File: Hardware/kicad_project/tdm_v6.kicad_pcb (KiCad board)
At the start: 4 copper layers, 65 x 100 mm, 139 parts, among them J1 line_in, J2 headphone_out, J3 battery, J4 DebugHeader, Q1 DMG2305UX-13, SW1 spst_4_pin_internal, SW10 spst_4_pin_internal, SW11 spst_4_pin_internal, SW12 spst_4_pin_internal, SW13 spst_4_pin_internal, SW14 spst_4_pin_internal, SW15 spst_4_pin_internal, SW16 spst_4_pin_internal, SW17 spst_4_pin_internal, SW18 spst_4_pin_internal, SW19 spst_4_pin_internal, SW2 spst_4_pin_internal, SW20 spst_4_pin_internal, SW21 spst_4_pin_internal, SW22 spst_4_pin_internal, SW23 spst_4_pin_internal, SW24 spst_4_pin_internal, SW25 spst_4_pin_internal, SW26 spst_4_pin_internal, SW3 spst_4_pin_internal, SW4 spst_4_pin_internal, SW5 spst_4_pin_internal, SW6 spst_4_pin_internal, SW7 spst_4_pin_internal, SW8 spst_4_pin_internal, SW9 spst_4_pin_internal, U2 Pico, U3 TLV320AIC3204, U4 SPWmicrophone, U5 MCP73831T-2ATI_OT

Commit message: update project with corrected schematic / pcb
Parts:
- removed C2, C3, C4, C5: 1u, RandomJunk:C_0402_NoSilk
- removed D1, D2, D3, D4, D5: D, RandomJunk:D_SOD-323F_less_silk
- removed LS1: Speaker, RandomJunk:CMS-181325
- removed OL1: OLED, kbd:OLED_v2
- added C39: .47u, RandomJunk:C_0603_nosilk, F.Cu at (80.5, 40.8)
- added C40: .1uF, RandomJunk:C_0603_nosilk, F.Cu at (78.5, 44.2)
- added C41: 1u, RandomJunk:C_0402_NoSilk, F.Cu at (72.0, 51.4)
- added C42: 10u, RandomJunk:C_0402_NoSilk, F.Cu at (73.3, 44.1)
- added C43: 10u, RandomJunk:C_0402_NoSilk, F.Cu at (81.8, 47.1)
- added C44: .47u, RandomJunk:C_0603_nosilk, F.Cu at (73.5, 41.6)
- added C45: .47u, RandomJunk:C_0603_nosilk, F.Cu at (77.5, 54.0)
- added C46: 10u, RandomJunk:C_0402_NoSilk, F.Cu at (82.0, 50.5)
- added C47: .47u, RandomJunk:C_0603_nosilk, F.Cu at (85.2, 52.0)
- added C48: 47uf, Capacitors_SMD:C_1206, F.Cu at (83.3, 40.6)
- added C49: 47uf, Capacitors_SMD:C_1206, F.Cu at (90.2, 40.5)
- added C50: 10u, RandomJunk:C_0402_NoSilk, F.Cu at (40.5, 56.9)
- added C51: 1u, RandomJunk:C_0402_NoSilk, F.Cu at (47.8, 56.6)
- added C52: 1u, RandomJunk:C_0402_NoSilk, F.Cu at (38.8, 72.0)
- added C53: 1u, RandomJunk:C_0402_NoSilk, F.Cu at (38.8, 70.5)
- added C54: 1u, RandomJunk:C_0402_NoSilk, F.Cu at (43.2, 56.4)
- added C55: 10u, RandomJunk:C_0402_NoSilk, F.Cu at (52.8, 56.6)
- added C56: 10u, RandomJunk:C_0402_NoSilk, F.Cu at (49.0, 71.6)
- added C57: 10u, RandomJunk:C_0402_NoSilk, F.Cu at (48.6, 47.0)
- added C58: 10u, RandomJunk:C_0402_NoSilk, F.Cu at (40.2, 40.4)
- added D53: D_Schottky, Diodes_SMD:D_SMA, F.Cu at (56.5, 39.6)
- added D54: LED, LEDs:LED_0603, F.Cu at (57.8, 34.1)
- added J5: midi_in, RandomJunk:HRO-PJ-327C-A, B.Cu at (44.3, 40.6)
- added J6: midi_out, RandomJunk:HRO-PJ-327C-A, B.Cu at (54.3, 40.6)
- added J7: battery, Connectors_JST:JST_PH_B2B-PH-SM4-TB_02x2.00mm_Straight, B.Cu at (50.8, 52.1)
- added LCD1: 128x32OLED, RandomJunk:oled_ssd1306_14pin_91, F.Cu at (43.3, 62.1)
- added R10: 220, RandomJunk:R_0402_NoSilk, F.Cu at (40.7, 44.5)
- added R11: 1k, RandomJunk:R_0402_NoSilk, F.Cu at (44.5, 56.5)
- added R12: 220, RandomJunk:R_0402_NoSilk, F.Cu at (50.2, 37.6)
- added R13: 220, RandomJunk:R_0402_NoSilk, F.Cu at (56.0, 42.0)
- added R14: 10k, RandomJunk:R_0402_NoSilk, F.Cu at (50.3, 56.6)
- added R15: 330k, RandomJunk:R_0402_NoSilk, F.Cu at (48.5, 70.1)
- added R16: 4.7k, RandomJunk:R_0402_NoSilk, F.Cu at (52.4, 42.9)
- added R17: 1k, RandomJunk:R_0402_NoSilk, F.Cu at (55.8, 33.1)
- added R18: 100k, RandomJunk:R_0402_NoSilk, F.Cu at (52.4, 44.0)
- added R19: 5.1k, RandomJunk:R_0402_NoSilk, F.Cu at (66.8, 42.1)
- added R20: 5.1k, RandomJunk:R_0402_NoSilk, F.Cu at (63.3, 42.1)
- added R7: 1k, RandomJunk:R_0402_NoSilk, F.Cu at (67.5, 48.4)
- added R8: 1k, RandomJunk:R_0402_NoSilk, F.Cu at (59.8, 42.5)
- added R9: 4.7k, RandomJunk:R_0402_NoSilk, F.Cu at (79.5, 53.8)
- added SW27: spst_4_pin_internal, RandomJunk:ts1102_smallerpads_buttonhole, B.Cu at (60.8, 67.6)
- added U1: W25Q32JVSS, Housings_SOIC:SOIJ-8_5.3x5.3mm_Pitch1.27mm, F.Cu at (49.7, 50.5)
- added U6: MCP73831T-2ATI_OT, TO_SOT_Packages_SMD:SOT-23-5, F.Cu at (51.1, 40.4)
- added U7: AMS1117-3.3, TO_SOT_Packages_SMD:SOT-223, F.Cu at (44.4, 37.1)
- added Y1: Crystal_GND24, Crystals:Crystal_SMD_3225-4pin_3.2x2.5mm, F.Cu at (70.5, 48.5)
- C1: footprint RandomJunk:C_0402_NoSilk -> Capacitors_SMD:C_0402_NoSilk
- C26, C30, C31, C34: value 10u -> 100n; footprint RandomJunk:C_0603_nosilk -> RandomJunk:C_0402_NoSilk
- C27, C32: value .47u -> 100n; footprint RandomJunk:C_0603_nosilk -> RandomJunk:C_0402_NoSilk
- C28: value .1uF -> 100n; footprint RandomJunk:C_0603_nosilk -> RandomJunk:C_0402_NoSilk
- C29: value 1.0u -> 100n; footprint RandomJunk:C_0603_nosilk -> RandomJunk:C_0402_NoSilk
- C33: value .47u -> 1u; footprint RandomJunk:C_0603_nosilk -> RandomJunk:C_0402_NoSilk
- C35: value .47u -> 30p; footprint RandomJunk:C_0603_nosilk -> RandomJunk:C_0402_NoSilk
- C36: value 47uf -> 10u; footprint Capacitors_SMD:C_1206 -> RandomJunk:C_0402_NoSilk
- C37: value 47uf -> 30p; footprint Capacitors_SMD:C_1206 -> RandomJunk:C_0402_NoSilk
- C38: footprint RandomJunk:C_0603_nosilk -> RandomJunk:C_0402_NoSilk
- D10, D11, D12, D13, D14, D15, D16, D17, D18, D19, D20, D21, D22, D23, D24, D25, D6, D7, D8, D9: value D -> WS2812B; footprint RandomJunk:D_SOD-323F_less_silk -> RandomJunk:ws2812b-2020-lightpipe
- D26, D27, D28, D29, D30, D31, D32, D33, D34, D35, D36, D37, D38, D39, D40, D41, D42, D43, D44, D45, D46, D47, D48, D49, D50: value WS2812B -> D; footprint RandomJunk:ws2812b-2020-lightpipe -> RandomJunk:D_SOD-323F_less_silk
- D51: value D_Schottky -> LED; footprint Diodes_SMD:D_SMA -> LEDs:LED_0603
- D52: value LED -> D; footprint LEDs:LED_0603 -> RandomJunk:D_SOD-323F_less_silk
- J1: value line_in -> picoprobe_debug; footprint RandomJunk:HRO-PJ-327C-A -> RandomJunk:pico debug header; moved to B.Cu
- J2: value headphone_out -> USB_C_Receptacle_USB2.0; footprint RandomJunk:HRO-PJ-327C-A -> RandomJunk:USB-C_SMD-TYPE-C-31-M-12
- J3: value battery -> line_in; footprint Connectors_JST:JST_PH_B2B-PH-SM4-TB_02x2.00mm_Straight -> RandomJunk:HRO-PJ-327C-A
- J4: value DebugHeader -> headphone_out; footprint Connector_PinSocket_2.54mm:PinSocket_1x04_P2.54mm_Vertical -> RandomJunk:HRO-PJ-327C-A
- R1, R2: value 4.7k -> 27.4; footprint Resistors_SMD:R_0603 -> RandomJunk:R_0402_NoSilk
- R3: value 4.7k -> DNF; footprint Resistors_SMD:R_0603 -> RandomJunk:R_0402_NoSilk
- R4: footprint Resistors_SMD:R_0603 -> RandomJunk:R_0402_NoSilk
- R5: value 1k -> 4.7k; footprint Resistors_SMD:R_0603 -> RandomJunk:R_0402_NoSilk
- R6: value 100k -> 1k; footprint Resistors_SMD:R_0603 -> RandomJunk:R_0402_NoSilk
- RV1, RV2: footprint RandomJunk:rk10j -> Potentiometers:Potentiometer_Alps_RK09K_Horizontal; moved to F.Cu
- SW26: moved to B.Cu
- U2: value Pico -> RP2040; footprint RandomJunk:RPi_Pico_SMD_only -> MCU_RaspberryPi_and_Boards:RP2040-QFN-56; moved to F.Cu
- U4: value SPWmicrophone -> AP3722AT_mic; footprint RandomJunk:SPW2430HR5H-B -> RandomJunk:AP3722AT-SMD-mic
- U5: value MCP73831T-2ATI_OT -> 6N137; footprint TO_SOT_Packages_SMD:SOT-23-5 -> Housings_SOIC:SO-8_5.3x6.2mm_Pitch1.27mm
- moved J1 93.6 mm to (65.8, 130.0), turned to 0 degrees
- moved H1 92.4 mm to (37.3, 128.1)
- moved H3 92.4 mm to (94.3, 128.1)
- moved H2 91.7 mm to (37.3, 35.6)
- moved H4 91.7 mm to (94.3, 35.6)
- moved U4 48.2 mm to (88.7, 50.6), turned to 90 degrees
- moved U5 48.0 mm to (39.2, 51.3), turned to 270 degrees
- moved J4 43.6 mm to (86.8, 40.6)
- moved RV1 39.1 mm to (73.8, 56.1)
- moved D51 38.1 mm to (61.3, 42.6), turned to 270 degrees
- moved Q1 36.8 mm to (49.2, 44.4), turned to 270 degrees
- moved SW26 32.0 mm to (60.8, 60.6), turned to 180 degrees
- moved R6 31.9 mm to (55.8, 54.7), turned to 270 degrees
- moved R4 29.5 mm to (60.3, 55.6), turned to 90 degrees
- moved U3 29.3 mm to (76.8, 49.1), turned to 0 degrees
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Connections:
- C1 pad 1: +3V3 -> Net-(C1-Pad1)
- C26 pad 1: GND -> +3V3
- C26 pad 2: Net-(C26-Pad2) -> GND
- C27 pad 1: Net-(C27-Pad1) -> +3V3
- C27 pad 2: Net-(C27-Pad2) -> GND
- C31 pad 1: Net-(C31-Pad1) -> +3V3
- C32 pad 1: Net-(C32-Pad1) -> +3V3
- C32 pad 2: Net-(C32-Pad2) -> GND
- C33 pad 1: Net-(C33-Pad1) -> +3V3
- C33 pad 2: Net-(C33-Pad2) -> GND
- C34 pad 1: GND -> +3V3
- C34 pad 2: Net-(C34-Pad2) -> GND
- C35 pad 1: Net-(C35-Pad1) -> /XIN
- C35 pad 2: Net-(C35-Pad2) -> GND
- C36 pad 1: Net-(C36-Pad1) -> VBUS
- C36 pad 2: Net-(C36-Pad2) -> GND
- C37 pad 2: Net-(C37-Pad2) -> GND
- C38 pad 1: +BATT -> GND
- C38 pad 2: GND -> Net-(C38-Pad2)
- D10 pad 1: key_row2 -> Net-(D10-Pad1)
- D10 pad 2: Net-(D10-Pad2) -> GND
- D11 pad 1: key_row3 -> Net-(D11-Pad1)
- D11 pad 2: Net-(D11-Pad2) -> GND
- D12 pad 1: key_row3 -> Net-(D12-Pad1)
- D12 pad 2: Net-(D12-Pad2) -> GND
- D13 pad 1: key_row3 -> Net-(D13-Pad1)
- D13 pad 2: Net-(D13-Pad2) -> GND
- D14 pad 1: key_row3 -> Net-(D14-Pad1)
- D14 pad 2: Net-(D14-Pad2) -> GND
- D15 pad 1: key_row3 -> Net-(D15-Pad1)
- D15 pad 2: Net-(D15-Pad2) -> GND
- D16 pad 1: key_row4 -> Net-(D16-Pad1)
- D16 pad 2: Net-(D16-Pad2) -> GND
- D17 pad 1: key_row4 -> Net-(D17-Pad1)
- D17 pad 2: Net-(D17-Pad2) -> GND
- D18 pad 1: key_row4 -> Net-(D18-Pad1)
- D18 pad 2: Net-(D18-Pad2) -> GND
- D19 pad 1: key_row4 -> Net-(D19-Pad1)
- D19 pad 2: Net-(D19-Pad2) -> GND
- D20 pad 1: key_row4 -> Net-(D20-Pad1)
- D20 pad 2: Net-(D20-Pad2) -> GND
- D21 pad 1: key_row5 -> Net-(D21-Pad1)
- D21 pad 2: Net-(D21-Pad2) -> GND
- D22 pad 1: key_row5 -> Net-(D22-Pad1)
- D22 pad 2: Net-(D22-Pad2) -> GND
- D23 pad 1: key_row5 -> Net-(D23-Pad1)
- D23 pad 2: Net-(D23-Pad2) -> GND
- D24 pad 1: key_row5 -> Net-(D24-Pad1)
- D24 pad 2: Net-(D24-Pad2) -> GND
- D25 pad 1: key_row5 -> Net-(D25-Pad1)
- D25 pad 2: Net-(D25-Pad2) -> GND
- D26 pad 1: Net-(D26-Pad1) -> key_row1
- D26 pad 2: GND -> Net-(D26-Pad2)
- D27 pad 1: Net-(D27-Pad1) -> key_row1
- D27 pad 2: GND -> Net-(D27-Pad2)
- D28 pad 1: Net-(D28-Pad1) -> key_row1
- D28 pad 2: GND -> Net-(D28-Pad2)
- D29 pad 1: Net-(D29-Pad1) -> key_row1
- D29 pad 2: GND -> Net-(D29-Pad2)
- D30 pad 1: Net-(D30-Pad1) -> key_row1
- D30 pad 2: GND -> Net-(D30-Pad2)
- D31 pad 1: Net-(D31-Pad1) -> key_row2
- D31 pad 2: GND -> Net-(D31-Pad2)
- D32 pad 1: Net-(D32-Pad1) -> key_row2
- D32 pad 2: GND -> Net-(D32-Pad2)
- D33 pad 1: Net-(D33-Pad1) -> key_row2
- D33 pad 2: GND -> Net-(D33-Pad2)
- D34 pad 1: Net-(D34-Pad1) -> key_row2
- D34 pad 2: GND -> Net-(D34-Pad2)
- D35 pad 1: Net-(D35-Pad1) -> key_row2
- D35 pad 2: GND -> Net-(D35-Pad2)
- D36 pad 1: Net-(D36-Pad1) -> key_row3
- D36 pad 2: GND -> Net-(D36-Pad2)
- D37 pad 1: Net-(D37-Pad1) -> key_row3
- D37 pad 2: GND -> Net-(D37-Pad2)
- D38 pad 1: Net-(D38-Pad1) -> key_row3
- D38 pad 2: GND -> Net-(D38-Pad2)
- D39 pad 1: Net-(D39-Pad1) -> key_row3
- D39 pad 2: GND -> Net-(D39-Pad2)
- D40 pad 1: Net-(D40-Pad1) -> key_row3
- D40 pad 2: GND -> Net-(D40-Pad2)
- D41 pad 1: Net-(D41-Pad1) -> key_row4
- D41 pad 2: GND -> Net-(D41-Pad2)
- D42 pad 1: Net-(D42-Pad1) -> key_row4
- D42 pad 2: GND -> Net-(D42-Pad2)
- D43 pad 1: Net-(D43-Pad1) -> key_row4
- D43 pad 2: GND -> Net-(D43-Pad2)
- D44 pad 1: Net-(D44-Pad1) -> key_row4
- D44 pad 2: GND -> Net-(D44-Pad2)
- D45 pad 1: Net-(D45-Pad1) -> key_row4
- D45 pad 2: GND -> Net-(D45-Pad2)
- D46 pad 1: Net-(D46-Pad1) -> key_row5
- D46 pad 2: GND -> Net-(D46-Pad2)
- D47 pad 1: Net-(D47-Pad1) -> key_row5
- D47 pad 2: GND -> Net-(D47-Pad2)
- D48 pad 1: Net-(D48-Pad1) -> key_row5
- D48 pad 2: GND -> Net-(D48-Pad2)
- D49 pad 1: Net-(D49-Pad1) -> key_row5
- D49 pad 2: GND -> Net-(D49-Pad2)
- D50 pad 1: (no net) -> key_row5
- D50 pad 2: GND -> Net-(D50-Pad2)
- D51 pad 1: vsys -> Net-(D51-Pad1)
- D51 pad 2: VBUS -> Net-(D51-Pad2)
- D52 pad 2: VBUS -> Net-(D52-Pad2)
- D6 pad 1: key_row2 -> Net-(D6-Pad1)
- D6 pad 2: Net-(D6-Pad2) -> GND
- D7 pad 1: key_row2 -> Net-(D7-Pad1)
- D7 pad 2: Net-(D7-Pad2) -> GND
- D8 pad 1: key_row2 -> Net-(D8-Pad1)
- D8 pad 2: Net-(D8-Pad2) -> GND
- D9 pad 1: key_row2 -> Net-(D10-Pad3)
- D9 pad 2: Net-(D9-Pad2) -> GND
- J1 pad 2: Net-(C27-Pad2) -> swclk
- J1 pad 3: Net-(C32-Pad2) -> swdio
- J1 pad 4: (no net) -> rx
- J3 pad 1: +BATT -> GND
- J3 pad 2: GND -> Net-(C39-Pad2)
- J4 pad 1: Net-(J4-Pad1) -> GND
- J4 pad 2: Net-(J4-Pad2) -> Net-(C49-Pad1)
- J4 pad 3: Net-(J4-Pad3) -> Net-(C48-Pad1)
- Q1 pad 2: vsys -> Net-(D53-Pad1)
- R1 pad 1: +3V3 -> Net-(R1-Pad1)
- R1 pad 2: sda -> /USB_D+
- R2 pad 1: +3V3 -> Net-(R2-Pad1)
- R2 pad 2: scl -> /USB_D-
- R3 pad 1: Net-(C33-Pad2) -> +3V3
- R3 pad 2: Net-(R3-Pad2) -> /QSPI_SS
- R4 pad 1: Net-(R4-Pad1) -> +3V3
- R4 pad 2: GND -> sda
- R5 pad 1: Net-(D52-Pad1) -> +3V3
- R5 pad 2: Net-(R5-Pad2) -> scl
- R6 pad 1: GND -> /QSPI_SS
- R6 pad 2: VBUS -> Net-(R6-Pad2)
- SW1 pad 1: Net-(D1-Pad2) -> Net-(D26-Pad2)
- SW1 pad 2: (no net) -> Net-(SW1-Pad2)
- SW10 pad 1: Net-(D10-Pad2) -> Net-(D35-Pad2)
- SW10 pad 2: (no net) -> Net-(SW10-Pad2)
- SW11 pad 1: Net-(D11-Pad2) -> Net-(D36-Pad2)
- SW11 pad 2: (no net) -> Net-(SW11-Pad2)
- SW12 pad 1: Net-(D12-Pad2) -> Net-(D37-Pad2)
- SW12 pad 2: (no net) -> Net-(SW12-Pad2)
- SW13 pad 1: Net-(D13-Pad2) -> Net-(D38-Pad2)
- SW13 pad 2: (no net) -> Net-(SW13-Pad2)
- SW14 pad 1: Net-(D14-Pad2) -> Net-(D39-Pad2)
- SW14 pad 2: (no net) -> Net-(SW14-Pad2)
- SW15 pad 1: Net-(D15-Pad2) -> Net-(D40-Pad2)
- SW15 pad 2: (no net) -> Net-(SW15-Pad2)
- SW16 pad 1: Net-(D16-Pad2) -> Net-(D41-Pad2)
- SW16 pad 2: (no net) -> Net-(SW16-Pad2)
- SW17 pad 1: Net-(D17-Pad2) -> Net-(D42-Pad2)
- SW17 pad 2: (no net) -> Net-(SW17-Pad2)
- SW18 pad 1: Net-(D18-Pad2) -> Net-(D43-Pad2)
- SW18 pad 2: (no net) -> Net-(SW18-Pad2)
- SW19 pad 1: Net-(D19-Pad2) -> Net-(D44-Pad2)
- SW19 pad 2: (no net) -> Net-(SW19-Pad2)
- SW2 pad 1: Net-(D2-Pad2) -> Net-(D27-Pad2)
- SW2 pad 2: (no net) -> Net-(SW2-Pad2)
- SW20 pad 1: Net-(D20-Pad2) -> Net-(D45-Pad2)
- SW20 pad 2: (no net) -> Net-(SW20-Pad2)
- SW21 pad 1: Net-(D21-Pad2) -> Net-(D46-Pad2)
- SW21 pad 2: (no net) -> Net-(SW21-Pad2)
- SW21 pad 3: (no net) -> Net-(SW21-Pad3)
- SW22 pad 1: Net-(D22-Pad2) -> Net-(D47-Pad2)
- SW22 pad 2: (no net) -> Net-(SW22-Pad2)
- SW22 pad 3: (no net) -> Net-(SW22-Pad3)
- SW23 pad 1: Net-(D23-Pad2) -> Net-(D48-Pad2)
- SW23 pad 2: (no net) -> Net-(SW23-Pad2)
- SW23 pad 3: (no net) -> Net-(SW23-Pad3)
- SW24 pad 1: Net-(D24-Pad2) -> Net-(D49-Pad2)
- SW24 pad 2: (no net) -> Net-(SW24-Pad2)
- SW24 pad 3: (no net) -> Net-(SW24-Pad3)
- SW25 pad 1: Net-(D25-Pad2) -> Net-(D50-Pad2)
- SW25 pad 2: (no net) -> Net-(SW25-Pad2)
- SW25 pad 3: (no net) -> Net-(SW25-Pad3)
- SW26 pad 2: (no net) -> Net-(R6-Pad2)
- SW26 pad 4: (no net) -> Net-(SW26-Pad4)
- SW3 pad 1: Net-(D3-Pad2) -> Net-(D28-Pad2)
- SW3 pad 2: (no net) -> Net-(SW3-Pad2)
- SW4 pad 1: Net-(D4-Pad2) -> Net-(D29-Pad2)
- SW4 pad 2: (no net) -> Net-(SW4-Pad2)
- SW5 pad 1: Net-(D5-Pad2) -> Net-(D30-Pad2)
- SW5 pad 2: (no net) -> Net-(SW5-Pad2)
- SW6 pad 1: Net-(D6-Pad2) -> Net-(D31-Pad2)
- SW6 pad 2: (no net) -> Net-(SW6-Pad2)
- SW7 pad 1: Net-(D7-Pad2) -> Net-(D32-Pad2)
- SW7 pad 2: (no net) -> Net-(SW7-Pad2)
- SW8 pad 1: Net-(D8-Pad2) -> Net-(D33-Pad2)
- SW8 pad 2: (no net) -> Net-(SW8-Pad2)
- SW9 pad 1: Net-(D9-Pad2) -> Net-(D34-Pad2)
- SW9 pad 2: (no net) -> Net-(SW9-Pad2)
- U2 pad 1: Net-(J4-Pad4) -> +3V3
- U2 pad 10: key_col2 -> +3V3
- U2 pad 13: (no net) -> key_col5
- U2 pad 14: key_col5 -> key_row1
- U2 pad 15: key_row1 -> key_row2
- U2 pad 16: key_row2 -> key_row3
- U2 pad 17: key_row3 -> key_row4
- U2 pad 18: (no net) -> key_row5
- U2 pad 19: key_row4 -> GND
- U2 pad 2: Net-(J4-Pad3) -> tx
- U2 pad 20: key_row5 -> /XIN
- U2 pad 21: mclk -> /XOUT
- U2 pad 22: bck -> +3V3
- U2 pad 23: GND -> Net-(C1-Pad1)
- U2 pad 24: lrclk -> swclk
- U2 pad 25: din -> swdio
- U2 pad 26: dout -> Net-(SW27-Pad1)
- U2 pad 27: codec_reset -> mclk
- U2 pad 28: GND -> bck
- U2 pad 29: (no net) -> lrclk
- U2 pad 3: (no net) -> rx
- U2 pad 30: Net-(SW26-Pad1) -> din
- U2 pad 31: pot1 -> dout
- U2 pad 32: pot2 -> codec_reset
- U2 pad 33: (no net) -> +3V3
- U2 pad 34: (no net) -> led_din
- U2 pad 35: (no net) -> Net-(U2-Pad35)
- U2 pad 36: +3V3 -> Net-(U2-Pad36)
- U2 pad 37: (no net) -> Net-(D51-Pad2)
- U2 pad 38: GND -> pot1
- U2 pad 39: vsys -> pot2
- U2 pad 40: VBUS -> Net-(U2-Pad40)
- U2 pad 41: Net-(J4-Pad2) -> Net-(U2-Pad41)
- U2 pad 42: (no net) -> +3V3
- U2 pad 43: Net-(J4-Pad1) -> +3V3
- U2 pad 6: led_din -> /MIDI_TX
- U2 pad 7: (no net) -> /MIDI_RX
- U2 pad 8: (no net) -> key_col1
- U2 pad 9: key_col1 -> key_col2
- U3 pad 11: (no net) -> Net-(U3-Pad11)
- U3 pad 13: Net-(C27-Pad1) -> Net-(C39-Pad1)
- U3 pad 14: Net-(C32-Pad1) -> Net-(C44-Pad1)
- U3 pad 15: Net-(C33-Pad1) -> Net-(C45-Pad1)
- U3 pad 16: Net-(C35-Pad1) -> Net-(C47-Pad1)
- U3 pad 18: Net-(C34-Pad2) -> Net-(C46-Pad2)
- U3 pad 19: Net-(R3-Pad2) -> Net-(R9-Pad2)
- U3 pad 20: (no net) -> Net-(U3-Pad20)
- U3 pad 21: (no net) -> Net-(U3-Pad21)
- U3 pad 22: (no net) -> Net-(U3-Pad22)
- U3 pad 23: (no net) -> Net-(U3-Pad23)
- U3 pad 24: Net-(C31-Pad1) -> Net-(C43-Pad1)
- U3 pad 25: Net-(C37-Pad2) -> Net-(C49-Pad2)
- U3 pad 27: Net-(C36-Pad2) -> Net-(C48-Pad2)
- U3 pad 29: Net-(C26-Pad2) -> Net-(C38-Pad2)
- U3 pad 32: (no net) -> Net-(U3-Pad32)
- U3 pad 8: (no net) -> Net-(U3-Pad8)
- U4 pad 1: GND -> Net-(C45-Pad2)
- U4 pad 2: Net-(C33-Pad2) -> GND
- U4 pad 3: Net-(C35-Pad2) -> GND
- U4 pad 4: (no net) -> Net-(C47-Pad2)
- U5 pad 1: Net-(R5-Pad2) -> Net-(U5-Pad1)
- U5 pad 2: GND -> Net-(D52-Pad1)
- U5 pad 3: +BATT -> Net-(D52-Pad2)
- U5 pad 4: VBUS -> Net-(U5-Pad4)
- U5 pad 5: Net-(R4-Pad1) -> GND
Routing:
- net +3V3: track 140.2 -> 354.0 mm, vias 53 -> 46
- net swdio: track 0.00 -> 94.1 mm, vias 0 -> 2
- net tx: track 0.00 -> 90.6 mm, vias 0 -> 1
- net rx: track 0.00 -> 89.7 mm, vias 0 -> 1
- net swclk: track 0.00 -> 89.1 mm, vias 0 -> 2
- net scl: track 127.5 -> 45.2 mm
- net Net-(D30-Pad1): track 70.9 -> 0.00 mm
- net GND: track 167.6 -> 238.4 mm, vias 34 -> 22
- net Net-(D35-Pad1): track 60.6 -> 0.00 mm, vias 2 -> 0
- net Net-(D45-Pad1): track 60.1 -> 0.00 mm, vias 2 -> 0
- net vsys: track 56.5 -> 0.00 mm, vias 3 -> 0
- net Net-(J4-Pad2): track 55.8 -> 0.00 mm, vias 4 -> 0
- net Net-(D40-Pad1): track 54.3 -> 0.00 mm, vias 2 -> 0
- net Net-(D20-Pad1): track 0.00 -> 53.3 mm
- net Net-(D15-Pad1): track 0.00 -> 53.3 mm
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- added copper zone on B.Cu, net +3V3
- added copper zone on B.Cu, net GND
- added copper zone on F.Cu, net GND
- added copper zone on In2.Cu, net GND
- removed copper zone on In2.Cu, net +3V3
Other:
- outline, holes or cut-outs redrawn
- rule trace_min: 0.2 -> 0.09
- rule via_min_drill: 0.3 -> 0.2
- board text added: "+"
- board text added: "Audio In"
- board text added: "Audio Out"
- board text added: "RUN"
- board text added: "SAFEBOOT"
- board text added: "audio codec"
- board text added: "battery"
- board text added: "charge indicator"
- board text added: "crystal"
- board text added: "mcu"
- board text added: "memory"
- board text added: "mic ro phone"
- board text added: "midi optoiso"
- board text added: "power"

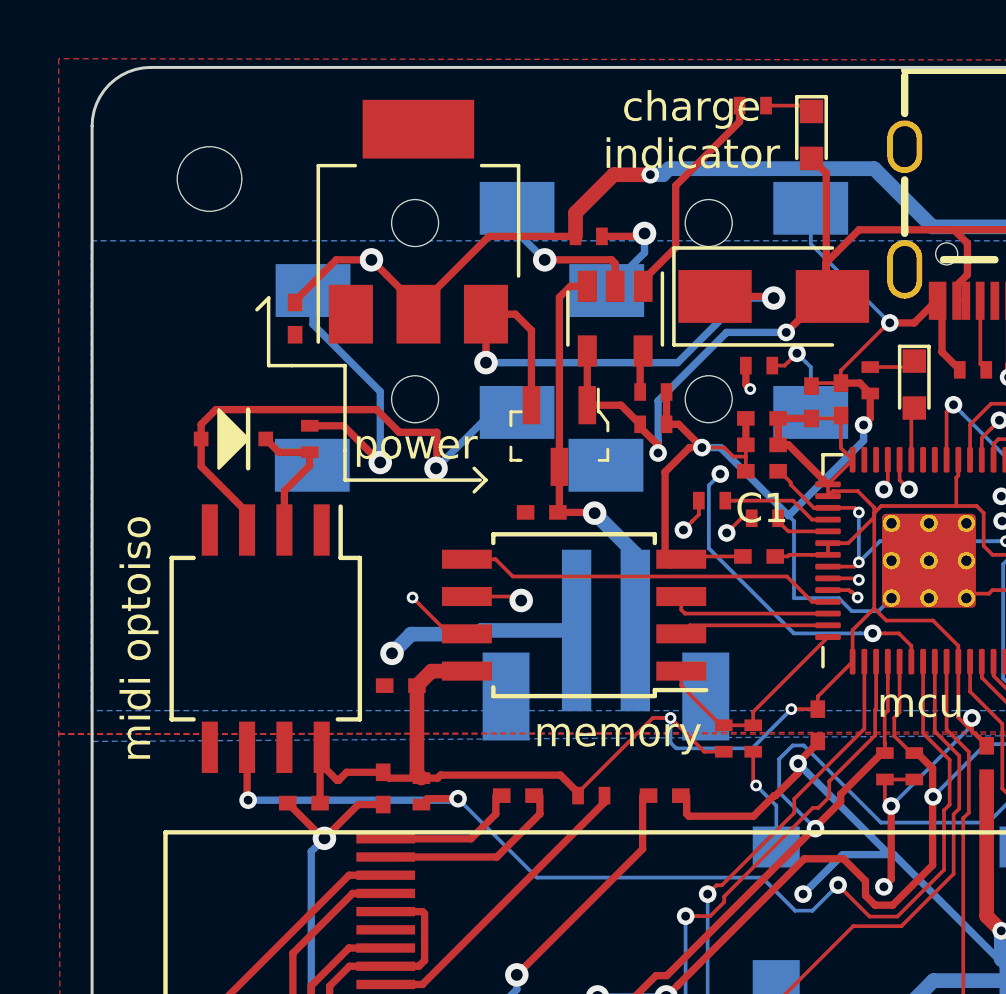
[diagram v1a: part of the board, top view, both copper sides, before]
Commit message: initial firmware commit, update hardware
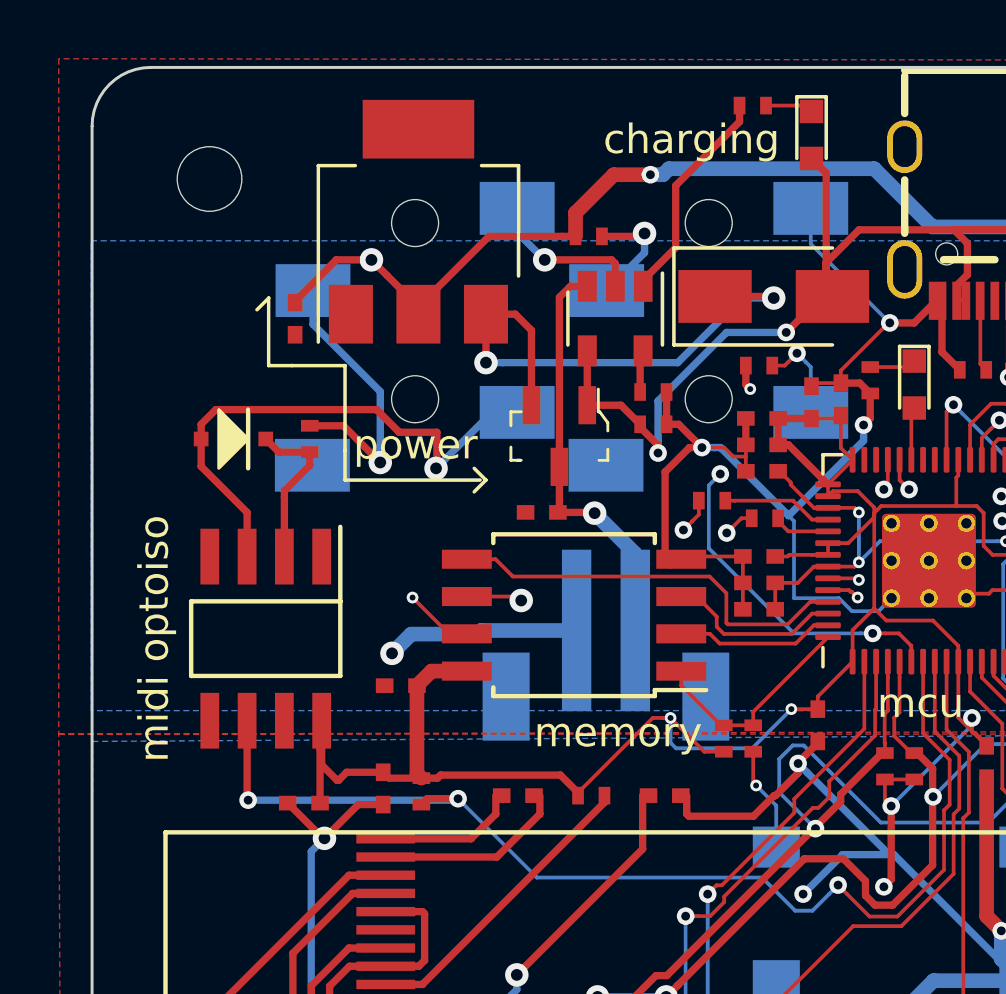
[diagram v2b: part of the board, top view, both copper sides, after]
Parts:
- added C2: 100n, Capacitors_SMD:C_0402_NoSilk, F.Cu at (56.0, 50.3)
- added C3: 100n, Capacitors_SMD:C_0402_NoSilk, F.Cu at (56.0, 49.4)
- U5: footprint Housings_SOIC:SO-8_5.3x6.2mm_Pitch1.27mm -> RandomJunk:SOP-8_3.9x5.1x1.27P
- turned U5 to 180 degrees
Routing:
- net Net-(C1-Pad1): track 12.3 -> 15.3 mm
- net GND: track 238.4 -> 240.2 mm
- net /QSPI_SD0: track 12.9 -> 14.1 mm
- net /QSPI_SD2: track 5.50 -> 6.02 mm
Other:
- board text added: "charging"
- board text removed: "charge indicator"

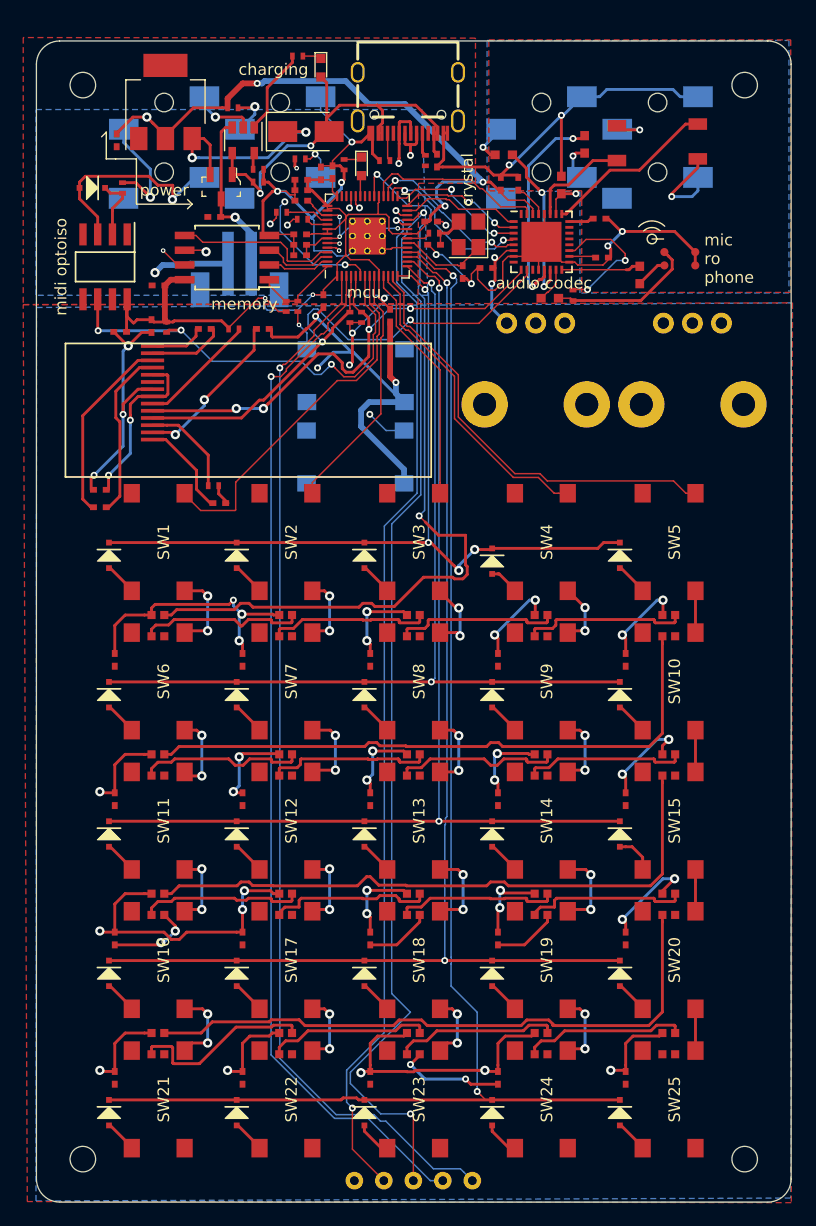
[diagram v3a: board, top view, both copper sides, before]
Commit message: new hardware rev
- soft / latching power switch
- corrected mic
- added pullup to flash ss
- front & back enclosure plates
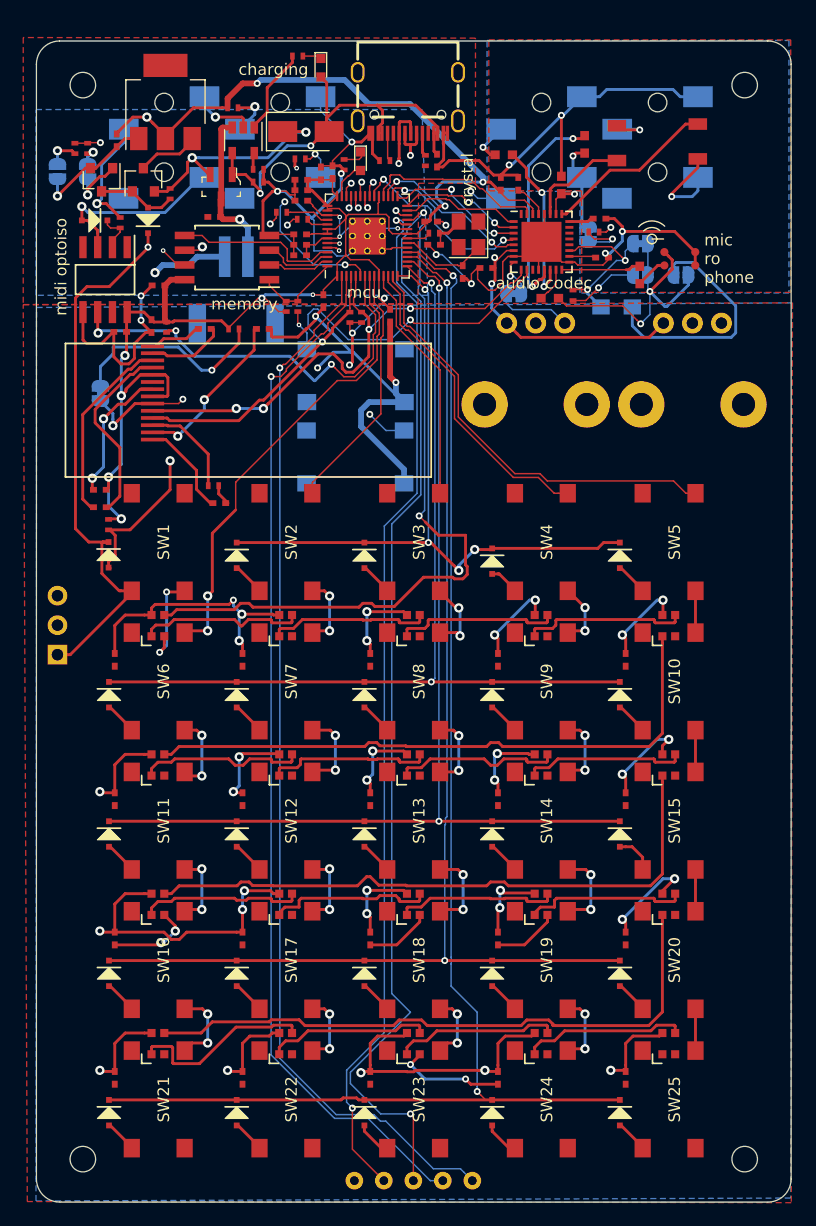
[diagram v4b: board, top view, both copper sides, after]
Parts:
- removed D26: D, RandomJunk:D_SOD-323F_less_silk
- added D1: D, RandomJunk:D_SOD-323F_less_silk, F.Cu at (42.9, 47.3)
- added D2: D, RandomJunk:D_SOD-323F_less_silk, F.Cu at (39.5, 76.1)
- added J8: Conn_01x03_Male, Connector_PinHeader_2.54mm:PinHeader_1x03_P2.54mm_Horizontal, B.Cu at (35.1, 84.7)
- added JP1: SolderJumper_2_Bridged, Jumper:SolderJumper-2_P1.3mm_Bridged_RoundedPad1.0x1.5mm, B.Cu at (80.8, 48.5)
- added JP2: SolderJumper_2_Bridged, Jumper:SolderJumper-2_P1.3mm_Bridged_RoundedPad1.0x1.5mm, B.Cu at (74.4, 53.6)
- added JP3: SolderJumper_2_Open, Jumper:SolderJumper-2_P1.3mm_Open_RoundedPad1.0x1.5mm, B.Cu at (85.3, 52.0)
- added JP4: SolderJumper_2_Bridged, Jumper:SolderJumper-2_P1.3mm_Bridged_RoundedPad1.0x1.5mm, B.Cu at (85.3, 49.3)
- added JP5: SolderJumper_2_Open, Jumper:SolderJumper-2_P1.3mm_Open_RoundedPad1.0x1.5mm, B.Cu at (88.8, 52.0)
- added JP6: SolderJumper_2_Bridged, Jumper:SolderJumper-2_P1.3mm_Bridged_RoundedPad1.0x1.5mm, B.Cu at (38.8, 62.2)
- added JP7: SolderJumper_2_Bridged, Jumper:SolderJumper-2_P1.3mm_Bridged_RoundedPad1.0x1.5mm, B.Cu at (37.7, 43.1)
- added JP8: SolderJumper_2_Open, Jumper:SolderJumper-2_P1.3mm_Open_RoundedPad1.0x1.5mm, B.Cu at (35.1, 43.1)
- added Q2: Q_PMOS_GSD, TO_SOT_Packages_SMD:SOT-23, F.Cu at (42.5, 43.8)
- added Q3: Q_NPN_BEC, TO_SOT_Packages_SMD:SOT-23, F.Cu at (38.9, 43.8)
- added R21: 100k, Resistors_SMD:R_0402_NoSilk, F.Cu at (44.8, 45.0)
- added R22: 100k, Resistors_SMD:R_0402_NoSilk, F.Cu at (39.5, 73.5)
- added R23: 100k, Resistors_SMD:R_0402_NoSilk, F.Cu at (37.7, 41.1)
- added R24: 10k, Resistors_SMD:R_0402_NoSilk, F.Cu at (81.3, 48.3)
- added R25: dnf, Resistors_SMD:R_0805_HandSoldering, B.Cu at (83.3, 54.8)
- added R26: 10k, Resistors_SMD:R_0402_NoSilk, F.Cu at (36.6, 41.1)
- J7: footprint Connectors_JST:JST_PH_B2B-PH-SM4-TB_02x2.00mm_Straight -> Connectors_JST:JST_PH_S2B-PH-SM4-TB_02x2.00mm_Angled
- R3: value DNF -> 10k
- R9: value 4.7k -> 1k
- moved R10 3.01 mm to (40.5, 47.5)
- moved D52 2.81 mm to (38.3, 47.3)
- moved J7 1.19 mm to (50.5, 53.3), turned to 180 degrees
- moved U5 1.10 mm to (39.2, 52.4)
- moved D51 0.45 mm to (61.2, 42.2)
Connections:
- J3 pad 4: Net-(J3-Pad4) -> line_in_detect
- LCD1 pad 9: Net-(LCD1-Pad9) -> screen_reset
- R14 pad 1: Net-(LCD1-Pad9) -> Net-(JP6-Pad1)
- R9 pad 1: Net-(C45-Pad2) -> Net-(JP3-Pad1)
- SW1 pad 3: Net-(SW1-Pad3) -> GND
- SW1 pad 4: key_col1 -> Net-(SW1-Pad4)
- SW6 pad 4: Net-(SW1-Pad3) -> key_col1
- U2 pad 35: Net-(U2-Pad35) -> latch_power
- U2 pad 36: Net-(U2-Pad36) -> power_gpio
- U2 pad 37: Net-(D51-Pad2) -> line_in_detect
- U2 pad 40: Net-(U2-Pad40) -> screen_reset
- U2 pad 41: Net-(U2-Pad41) -> Net-(D51-Pad2)
- U7 pad 3: Net-(D53-Pad1) -> Net-(Q2-Pad3)
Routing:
- net Net-(D1-Pad1): track 2.83 -> 47.8 mm, vias 0 -> 1
- net power_gpio: track 0.00 -> 44.9 mm, vias 0 -> 2
- net screen_reset: track 0.00 -> 35.7 mm, vias 0 -> 3
- net GND: track 240.2 -> 274.8 mm, vias 22 -> 26
- net +3V3: track 354.0 -> 384.9 mm, vias 46 -> 49
- net latch_power: track 0.00 -> 28.5 mm, vias 0 -> 2
- net Net-(JP5-Pad1): track 0.00 -> 21.3 mm
- net Net-(JP6-Pad1): track 0.00 -> 17.7 mm, vias 0 -> 1
- net line_in_detect: track 0.00 -> 14.5 mm, vias 0 -> 2
- net Net-(C45-Pad2): track 12.8 -> 25.2 mm, vias 0 -> 2
- net key_row1: track 71.0 -> 60.0 mm
- net Net-(LCD1-Pad9): track 10.2 -> 0.00 mm
- net key_col1: track 31.7 -> 40.1 mm, vias 0 -> 2
- net Net-(SW1-Pad3): track 7.22 -> 0.00 mm, vias 2 -> 0
- net Net-(D1-Pad2): track 0.00 -> 6.82 mm
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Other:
- board text added: "audio in"
- board text added: "audio out"
- board text removed: "Audio In"
- board text removed: "Audio Out"
- board text removed: "power"
